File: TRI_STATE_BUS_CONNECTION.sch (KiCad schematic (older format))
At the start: 2 parts

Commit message: way to long since last commit
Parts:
- gave numbers to parts that had none: 2
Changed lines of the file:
@@
 EESchema Schematic File Version 4
-LIBS:computer-cache
 EELAYER 30 0
 EELAYER END
 $Descr A4 11693 8268
 encoding utf-8
-Sheet 5 6
+Sheet 9 13
 Title ""
 Date ""
@@
 AR Path="/5D35D52D/5D399D3F/5D39F66E" Ref="#PWR?"  Part="1"
 AR Path="/5EE681E0/5EEF9D6A/5D39F66E" Ref="#PWR017"  Part="1"
-F 0 "#PWR?" H 3775 4750 50  0001 C CNN
+AR Path="/5F0705F7/5F16BEB4/5D39F66E" Ref="#PWR0121"  Part="1"
+AR Path="/5F0D7DA0/5F6363FD/5D39F66E" Ref="#PWR0129"  Part="1"
+F 0 "#PWR0129" H 3775 4750 50  0001 C CNN
 F 1 "GND" H 3780 4827 50  0000 C CNN
 F 2 "" H 3775 5000 50  0001 C CNN
@@
 AR Path="/5D35D52D/5D399D3F/5D39F67B" Ref="#PWR?"  Part="1"
 AR Path="/5EE681E0/5EEF9D6A/5D39F67B" Ref="#PWR016"  Part="1"
-F 0 "#PWR?" H 3575 4650 50  0001 C CNN
+AR Path="/5F0705F7/5F16BEB4/5D39F67B" Ref="#PWR0122"  Part="1"
+AR Path="/5F0D7DA0/5F6363FD/5D39F67B" Ref="#PWR0130"  Part="1"
+F 0 "#PWR0130" H 3575 4650 50  0001 C CNN
 F 1 "VCC" H 3592 4973 50  0000 C CNN
 F 2 "" H 3575 4800 50  0001 C CNN
@@
 	4875 5400 4875 6100
 $Comp
-L 74xx:74LS244 U?
+L 74xx:74LS244 U25
 U 1 1 5EC004DA
 P 4575 4900
-F 0 "U?" V 4529 5744 50  0000 L CNN
+F 0 "U25" V 4529 5744 50  0000 L CNN
 F 1 "74LS244" V 4620 5744 50  0000 L CNN
 F 2 "Package_DIP:DIP-20_W7.62mm_LongPads" H 4575 4900 50  0001 C CNN
@@
 	2375 4325 4075 4325
 $Comp
-L 74xx:74LS244 U?
+L 74xx:74LS244 U24
 U 1 1 5EC03675
 P 2775 4900
-F 0 "U?" V 2725 3975 50  0000 L CNN
+F 0 "U24" V 2725 3975 50  0000 L CNN
 F 1 "74LS244" V 2825 3750 50  0000 L CNN
 F 2 "Package_DIP:DIP-20_W7.62mm_LongPads" H 2775 4900 50  0001 C CNN
@@
 $EndComp
 $Comp
-L power:GND #PWR?
+L power:GND #PWR0131
 U 1 1 5EE83C06
 P 1975 5025
-F 0 "#PWR?" H 1975 4775 50  0001 C CNN
+F 0 "#PWR0131" H 1975 4775 50  0001 C CNN
 F 1 "GND" H 1980 4852 50  0000 C CNN
 F 2 "" H 1975 5025 50  0001 C CNN
@@
 $EndComp
 $Comp
-L power:VCC #PWR?
+L power:VCC #PWR0132
 U 1 1 5EE85163
 P 5375 4775
-F 0 "#PWR?" H 5375 4625 50  0001 C CNN
+F 0 "#PWR0132" H 5375 4625 50  0001 C CNN
 F 1 "VCC" H 5392 4948 50  0000 C CNN
 F 2 "" H 5375 4775 50  0001 C CNN

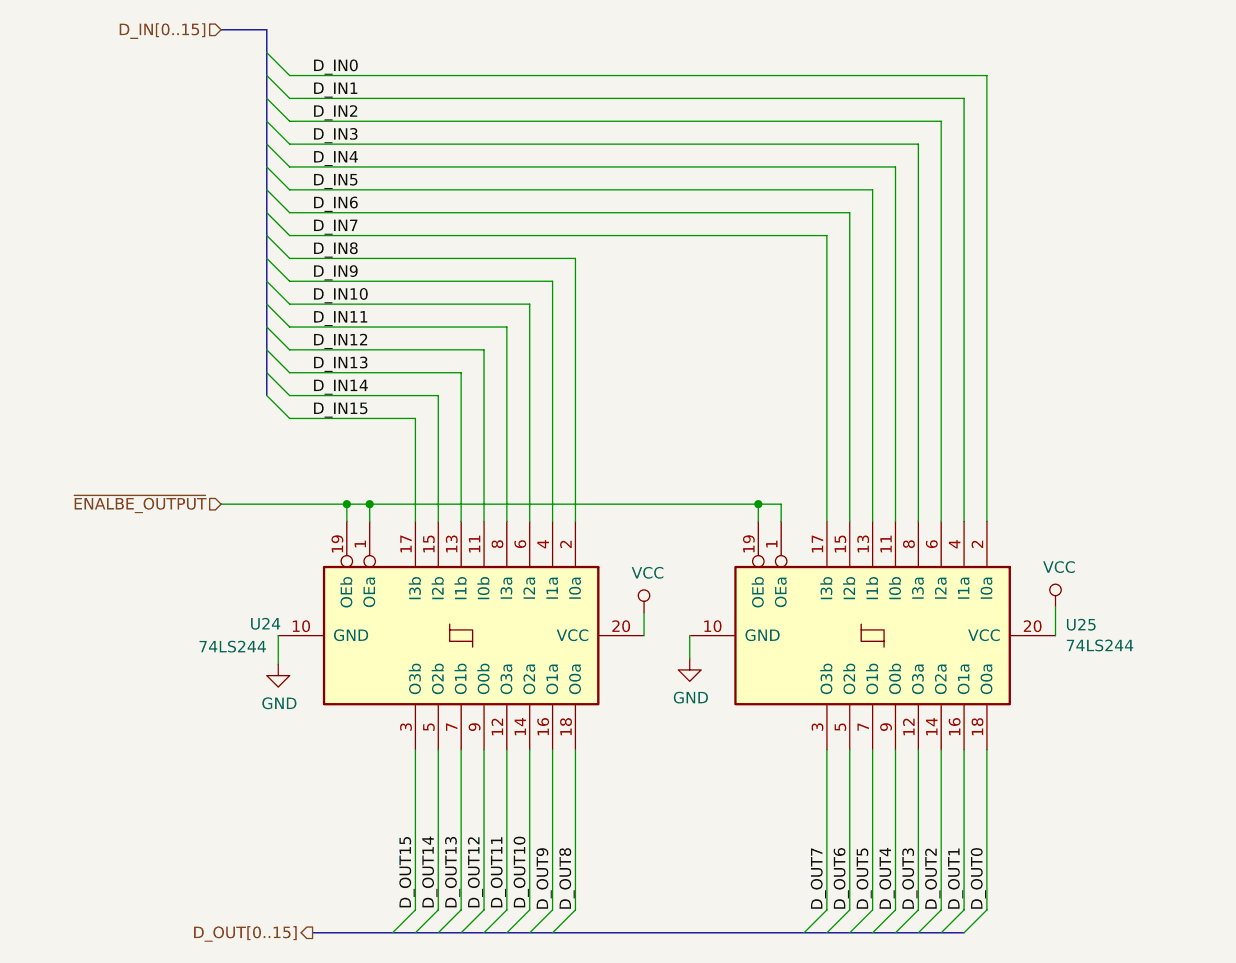
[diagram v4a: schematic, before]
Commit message: add bit operations
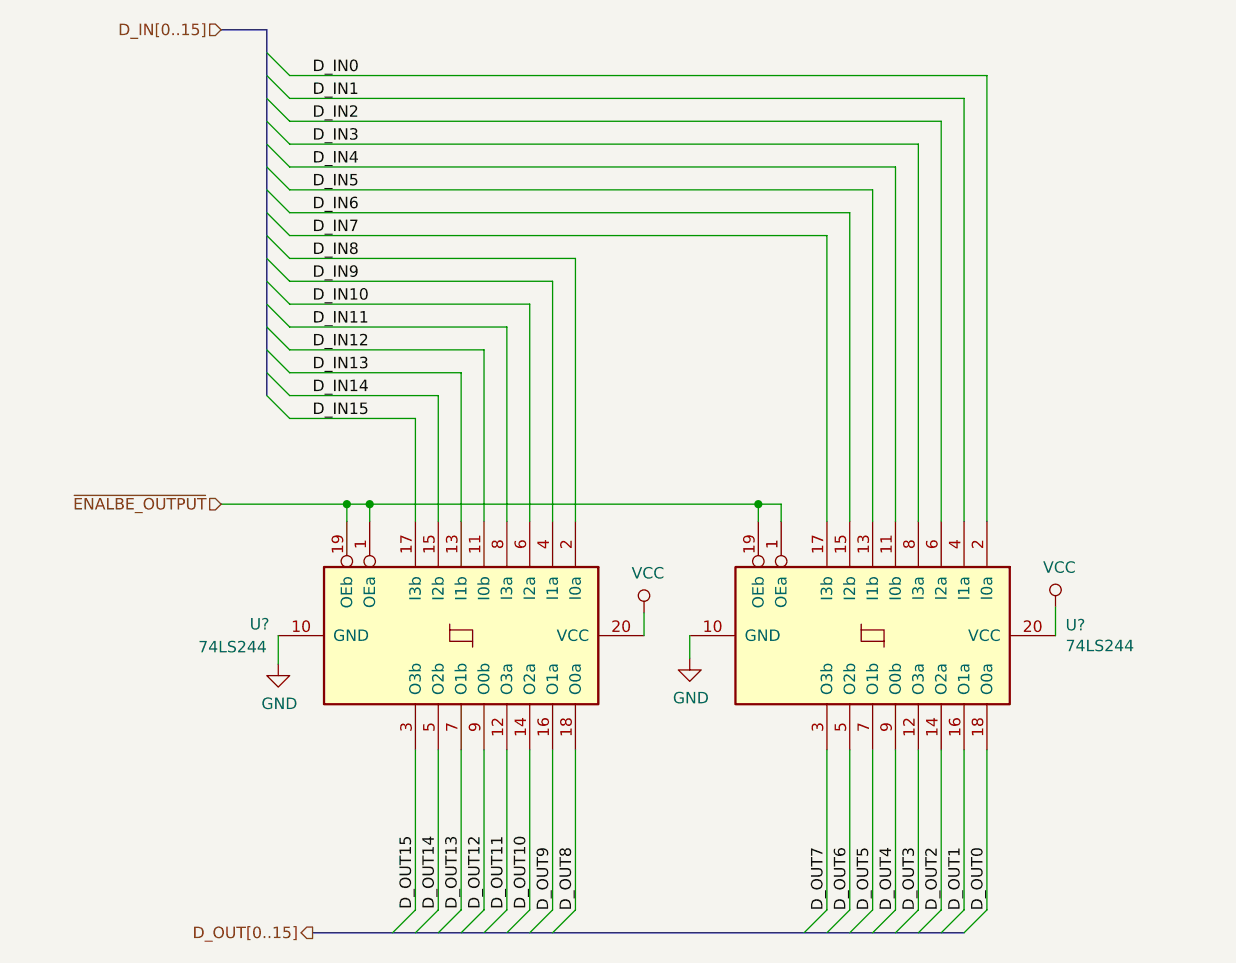
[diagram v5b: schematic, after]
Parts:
- renumbered U25 to U?, U24 to U?
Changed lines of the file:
@@
 EESchema Schematic File Version 4
+LIBS:computer-cache
 EELAYER 30 0
 EELAYER END
 $Descr A4 11693 8268
 encoding utf-8
-Sheet 9 13
+Sheet 4 29
 Title ""
 Date ""
@@
 AR Path="/5F0705F7/5F16BEB4/5D39F66E" Ref="#PWR0121"  Part="1"
 AR Path="/5F0D7DA0/5F6363FD/5D39F66E" Ref="#PWR0129"  Part="1"
-F 0 "#PWR0129" H 3775 4750 50  0001 C CNN
+AR Path="/5F287FC9/5F3E25CB/5D39F66E" Ref="#PWR013"  Part="1"
+F 0 "#PWR?" H 3775 4750 50  0001 C CNN
 F 1 "GND" H 3780 4827 50  0000 C CNN
 F 2 "" H 3775 5000 50  0001 C CNN
@@
 AR Path="/5F0705F7/5F16BEB4/5D39F67B" Ref="#PWR0122"  Part="1"
 AR Path="/5F0D7DA0/5F6363FD/5D39F67B" Ref="#PWR0130"  Part="1"
-F 0 "#PWR0130" H 3575 4650 50  0001 C CNN
+AR Path="/5F287FC9/5F3E25CB/5D39F67B" Ref="#PWR012"  Part="1"
+F 0 "#PWR?" H 3575 4650 50  0001 C CNN
 F 1 "VCC" H 3592 4973 50  0000 C CNN
 F 2 "" H 3575 4800 50  0001 C CNN
@@
 	4875 5400 4875 6100
 $Comp
-L 74xx:74LS244 U25
+L 74xx:74LS244 U?
 U 1 1 5EC004DA
 P 4575 4900
-F 0 "U25" V 4529 5744 50  0000 L CNN
+F 0 "U?" V 4529 5744 50  0000 L CNN
 F 1 "74LS244" V 4620 5744 50  0000 L CNN
 F 2 "Package_DIP:DIP-20_W7.62mm_LongPads" H 4575 4900 50  0001 C CNN
@@
 	2375 4325 4075 4325
 $Comp
-L 74xx:74LS244 U24
+L 74xx:74LS244 U?
 U 1 1 5EC03675
 P 2775 4900
-F 0 "U24" V 2725 3975 50  0000 L CNN
+F 0 "U?" V 2725 3975 50  0000 L CNN
 F 1 "74LS244" V 2825 3750 50  0000 L CNN
 F 2 "Package_DIP:DIP-20_W7.62mm_LongPads" H 2775 4900 50  0001 C CNN
@@
 $EndComp
 $Comp
-L power:GND #PWR0131
+L power:GND #PWR?
 U 1 1 5EE83C06
 P 1975 5025
-F 0 "#PWR0131" H 1975 4775 50  0001 C CNN
+F 0 "#PWR?" H 1975 4775 50  0001 C CNN
 F 1 "GND" H 1980 4852 50  0000 C CNN
 F 2 "" H 1975 5025 50  0001 C CNN
@@
 $EndComp
 $Comp
-L power:VCC #PWR0132
+L power:VCC #PWR?
 U 1 1 5EE85163
 P 5375 4775
-F 0 "#PWR0132" H 5375 4625 50  0001 C CNN
+F 0 "#PWR?" H 5375 4625 50  0001 C CNN
 F 1 "VCC" H 5392 4948 50  0000 C CNN
 F 2 "" H 5375 4775 50  0001 C CNN

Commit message: memory programmer and cu
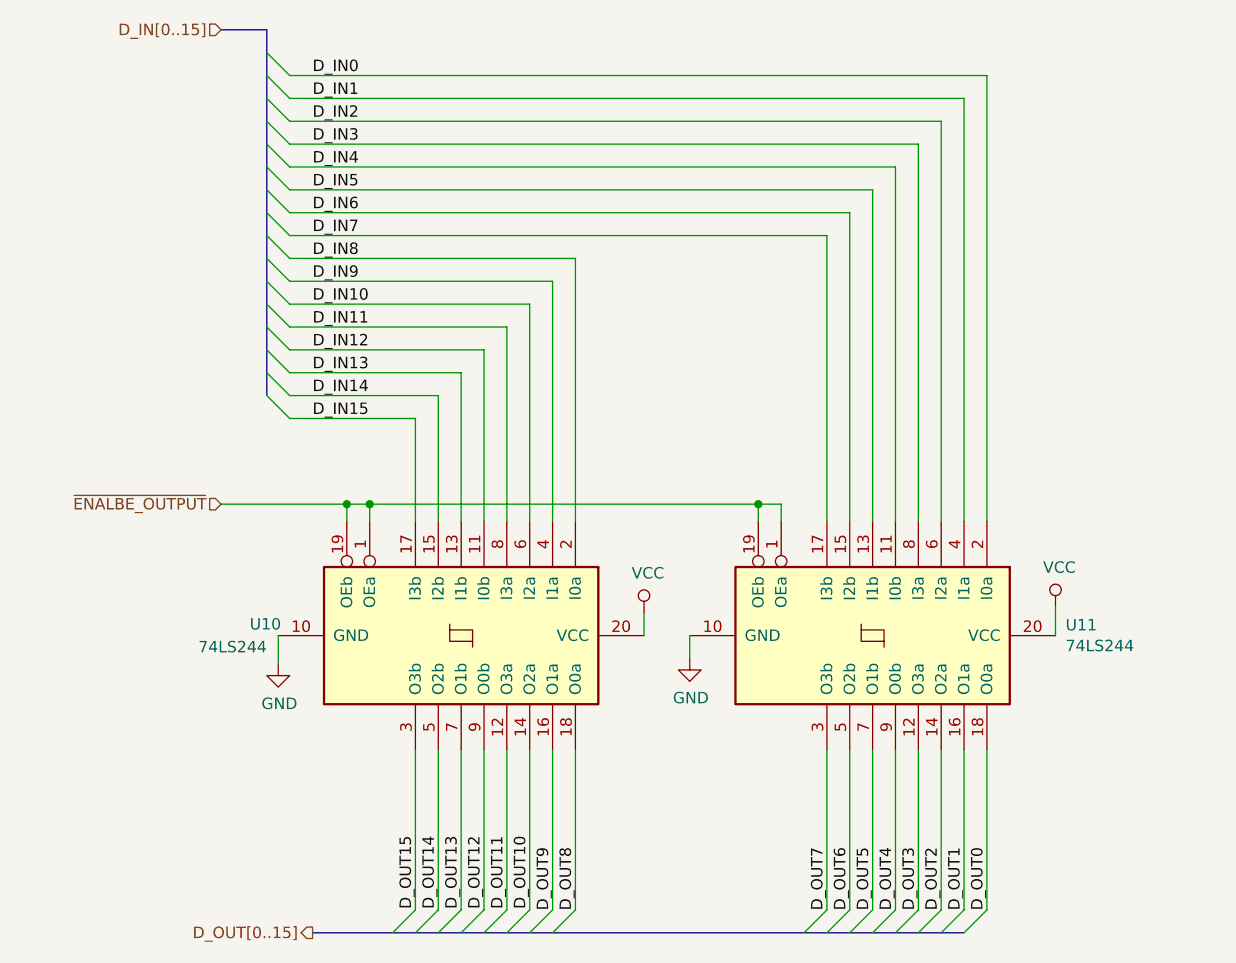
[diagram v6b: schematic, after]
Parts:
- gave numbers to parts that had none: 2
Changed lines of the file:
@@
 EESchema Schematic File Version 4
-LIBS:computer-cache
+LIBS:control_unit_pcb-cache
 EELAYER 30 0
 EELAYER END
 $Descr A4 11693 8268
 encoding utf-8
-Sheet 4 29
+Sheet 4 10
 Title ""
 Date ""
@@
 AR Path="/5F0D7DA0/5F6363FD/5D39F66E" Ref="#PWR0129"  Part="1"
 AR Path="/5F287FC9/5F3E25CB/5D39F66E" Ref="#PWR013"  Part="1"
-F 0 "#PWR?" H 3775 4750 50  0001 C CNN
+AR Path="/5F3AC91A/5F592F62/5D39F66E" Ref="#PWR0136"  Part="1"
+F 0 "#PWR0136" H 3775 4750 50  0001 C CNN
 F 1 "GND" H 3780 4827 50  0000 C CNN
 F 2 "" H 3775 5000 50  0001 C CNN
@@
 AR Path="/5F0D7DA0/5F6363FD/5D39F67B" Ref="#PWR0130"  Part="1"
 AR Path="/5F287FC9/5F3E25CB/5D39F67B" Ref="#PWR012"  Part="1"
-F 0 "#PWR?" H 3575 4650 50  0001 C CNN
+AR Path="/5F3AC91A/5F592F62/5D39F67B" Ref="#PWR0137"  Part="1"
+F 0 "#PWR0137" H 3575 4650 50  0001 C CNN
 F 1 "VCC" H 3592 4973 50  0000 C CNN
 F 2 "" H 3575 4800 50  0001 C CNN
@@
 	4875 5400 4875 6100
 $Comp
-L 74xx:74LS244 U?
+L 74xx:74LS244 U11
 U 1 1 5EC004DA
 P 4575 4900
-F 0 "U?" V 4529 5744 50  0000 L CNN
+F 0 "U11" V 4529 5744 50  0000 L CNN
 F 1 "74LS244" V 4620 5744 50  0000 L CNN
 F 2 "Package_DIP:DIP-20_W7.62mm_LongPads" H 4575 4900 50  0001 C CNN
@@
 	2375 4325 4075 4325
 $Comp
-L 74xx:74LS244 U?
+L 74xx:74LS244 U10
 U 1 1 5EC03675
 P 2775 4900
-F 0 "U?" V 2725 3975 50  0000 L CNN
+F 0 "U10" V 2725 3975 50  0000 L CNN
 F 1 "74LS244" V 2825 3750 50  0000 L CNN
 F 2 "Package_DIP:DIP-20_W7.62mm_LongPads" H 2775 4900 50  0001 C CNN
@@
 $EndComp
 $Comp
-L power:GND #PWR?
+L power:GND #PWR0138
 U 1 1 5EE83C06
 P 1975 5025
-F 0 "#PWR?" H 1975 4775 50  0001 C CNN
+F 0 "#PWR0138" H 1975 4775 50  0001 C CNN
 F 1 "GND" H 1980 4852 50  0000 C CNN
 F 2 "" H 1975 5025 50  0001 C CNN
@@
 $EndComp
 $Comp
-L power:VCC #PWR?
+L power:VCC #PWR0139
 U 1 1 5EE85163
 P 5375 4775
-F 0 "#PWR?" H 5375 4625 50  0001 C CNN
+F 0 "#PWR0139" H 5375 4625 50  0001 C CNN
 F 1 "VCC" H 5392 4948 50  0000 C CNN
 F 2 "" H 5375 4775 50  0001 C CNN

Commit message: part lists
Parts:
- renumbered U10 to U24, U11 to U25
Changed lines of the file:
@@
 EESchema Schematic File Version 4
-LIBS:bit_shifter_pcb-cache
+LIBS:program_counter_pcb-cache
 EELAYER 30 0
 EELAYER END
 $Descr A4 11693 8268
 encoding utf-8
-Sheet 4 6
+Sheet 5 6
 Title ""
 Date ""
@@
 AR Path="/5F287FC9/5F3E25CB/5D39F66E" Ref="#PWR013"  Part="1"
 AR Path="/5F3AC91A/5F592F62/5D39F66E" Ref="#PWR0136"  Part="1"
-F 0 "#PWR013" H 3775 4750 50  0001 C CNN
+F 0 "#PWR017" H 3775 4750 50  0001 C CNN
 F 1 "GND" H 3780 4827 50  0000 C CNN
 F 2 "" H 3775 5000 50  0001 C CNN
@@
 AR Path="/5F287FC9/5F3E25CB/5D39F67B" Ref="#PWR012"  Part="1"
 AR Path="/5F3AC91A/5F592F62/5D39F67B" Ref="#PWR0137"  Part="1"
-F 0 "#PWR012" H 3575 4650 50  0001 C CNN
+F 0 "#PWR016" H 3575 4650 50  0001 C CNN
 F 1 "VCC" H 3592 4973 50  0000 C CNN
 F 2 "" H 3575 4800 50  0001 C CNN
@@
 	4875 5400 4875 6100
 $Comp
-L 74xx:74LS244 U11
+L 74xx:74LS244 U25
 U 1 1 5EC004DA
 P 4575 4900
-F 0 "U11" V 4529 5744 50  0000 L CNN
+F 0 "U25" V 4529 5744 50  0000 L CNN
 F 1 "74LS244" V 4620 5744 50  0000 L CNN
 F 2 "Package_DIP:DIP-20_W7.62mm_LongPads" H 4575 4900 50  0001 C CNN
@@
 	2375 4325 4075 4325
 $Comp
-L 74xx:74LS244 U10
+L 74xx:74LS244 U24
 U 1 1 5EC03675
 P 2775 4900
-F 0 "U10" V 2725 3975 50  0000 L CNN
+F 0 "U24" V 2725 3975 50  0000 L CNN
 F 1 "74LS244" V 2825 3750 50  0000 L CNN
 F 2 "Package_DIP:DIP-20_W7.62mm_LongPads" H 2775 4900 50  0001 C CNN
